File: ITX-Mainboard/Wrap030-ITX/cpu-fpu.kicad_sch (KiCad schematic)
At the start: 36 parts, among them J2 Conn_01x03, U1 MC68882, X2 16M, X2 50M

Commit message: Schematic substantial completion
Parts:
- C1, C10, C11, C12, C13, C14, C2, C3, C31, C4, C5, C6, C7, C8, C9: footprint Capacitor_SMD:C_0805_2012Metric -> Capacitor_SMD:C_0402_1005Metric_Pad0.74x0.62mm_HandSolder; JLC-Part (none) -> https://jlcpcb.com/partdetail/1877-CL05B104KO5NNNC/C1525
- C15, C16: footprint Capacitor_SMD:C_0805_2012Metric -> Capacitor_SMD:C_0402_1005Metric_Pad0.74x0.62mm_HandSolder; JLC-Part (none) -> https://jlcpcb.com/partdetail/53938-CL05A105KA5NQNC/C52923
- J2: footprint (none) -> Connector_PinHeader_2.54mm:PinHeader_1x03_P2.54mm_Vertical
- RN1: Mouser-Part (none) -> 603-YC164-FR-071KL; Notes (none) -> 1k x4

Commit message: PCB substantial completion
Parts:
- added R2: 10k, Resistor_SMD:R_0805_2012Metric, symbol Device:R_Small_US
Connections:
- net FPU-CLK: now also J2.2 (Pin_2), U1.C2 (CLK); no longer J2.3 (Pin_3), X2.5 (OUT)
- net VCC: now also R2.2
- net ~{AVEC}: now also RN1.3 (R3.1); no longer RN1.4 (R4.1)
- net ~{BERR}: now also RN1.3 (R3.1); no longer RN1.1 (R1.1)
- net ~{CBACK}: now also RN1.1 (R1.1); no longer RN1.2 (R2.1)
- net ~{CDIS}: now also RN1.1 (R1.1); no longer RN1.1 (R1.1)
- net ~{CIIN}: now also RN1.2 (R2.1); no longer RN1.1 (R1.1)
- net ~{DSACK0}: now also RN1.4 (R4.1); no longer RN1.3 (R3.1), U1.J4 (~{DSACK0})
- net ~{DSACK1}: now also RN1.1 (R1.1); no longer RN1.4 (R4.1), U1.K4 (~{DSACK1})
- net ~{FPU-SENSE}: now also R2.1; no longer RN1.4 (R4.1)
- net ~{HALT}: now also RN1.4 (R4.1); no longer RN1.3 (R3.1)
- net ~{IPL0}: now also RN1.2 (R2.1); no longer RN1.1 (R1.1)
- net ~{IPL1}: now also RN1.4 (R4.1); no longer RN1.2 (R2.1)
- net ~{RESET}: now also RN1.1 (R1.1); no longer RN1.2 (R2.1)
- net ~{STERM}: now also RN1.2 (R2.1); no longer RN1.3 (R3.1)
- new net FPU-OSC: J2.3 (Pin_3), X2.5 (OUT)
- new net ~{BUS-DSACK0}: U1.J4 (~{DSACK0})
- new net ~{BUS-DSACK1}: U1.K4 (~{DSACK1})

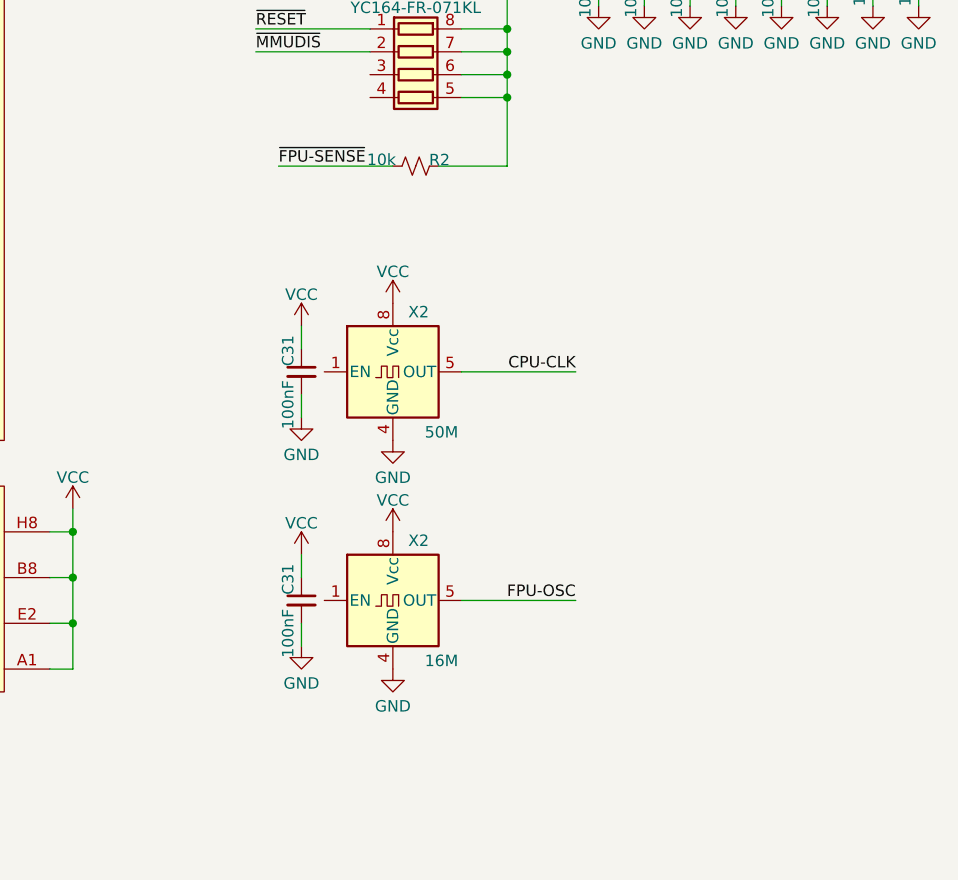
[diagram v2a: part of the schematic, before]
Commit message: Add interrupt controller to schematic
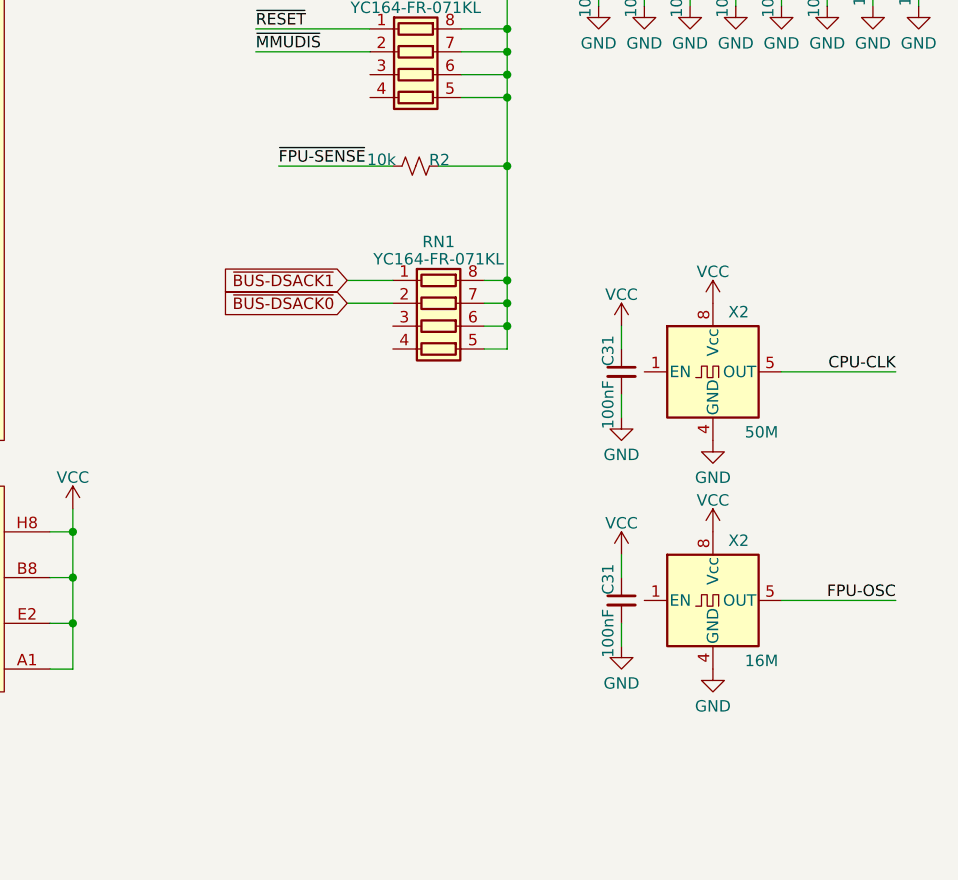
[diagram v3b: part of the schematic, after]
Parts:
- added RN1: YC164-FR-071KL, Resistor_SMD:R_Array_Convex_4x1206, symbol Device:R_Pack04
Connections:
- net VCC: now also RN1.5 (R4.2), RN1.6 (R3.2), RN1.7 (R2.2), RN1.8 (R1.2)
- net ~{BUS-DSACK0}: now also RN1.2 (R2.1)
- net ~{BUS-DSACK1}: now also RN1.1 (R1.1)
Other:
- moved on the sheet: C31, X2

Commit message: Completing PCB Routing
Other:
- title: Wrap030 ITX -> Wrap030-ATX Mainboard
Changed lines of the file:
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@@
   (paper "USLetter")
   (title_block
-    (title "Wrap030 ITX")
-    (date "2023-03-15")
-    (rev "0")
+    (title "Wrap030-ATX Mainboard")
+    (date "2023-03-26")
+    (rev "1")
     (company "techav")
   )

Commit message: initial production schematic
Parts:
- J2: value Conn_01x03 -> FPU CLK
- R2: JLC-Part (none) -> https://jlcpcb.com/partdetail/18102-0805W8F1002T5E/C17414
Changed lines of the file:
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@@
       (effects (font (size 1.27 1.27)))
     )
-    (property "Value" "Conn_01x03" (at 121.92 15.4211 0)
+    (property "Value" "FPU CLK" (at 121.92 15.4211 0)
       (effects (font (size 1.27 1.27)))
     )
@@
       (effects (font (size 1.27 1.27)) hide)
     )
-    (property "JLC-Part" "" (at 205.74 101.6 0)
-      (effects (font (size 1.27 1.27)) hide)
-    )
+    (property "JLC-Part" "https://jlcpcb.com/partdetail/18102-0805W8F1002T5E/C17414" (at 205.74 101.6 0)
+      (effects (font (size 1.27 1.27)) hide)
+    )

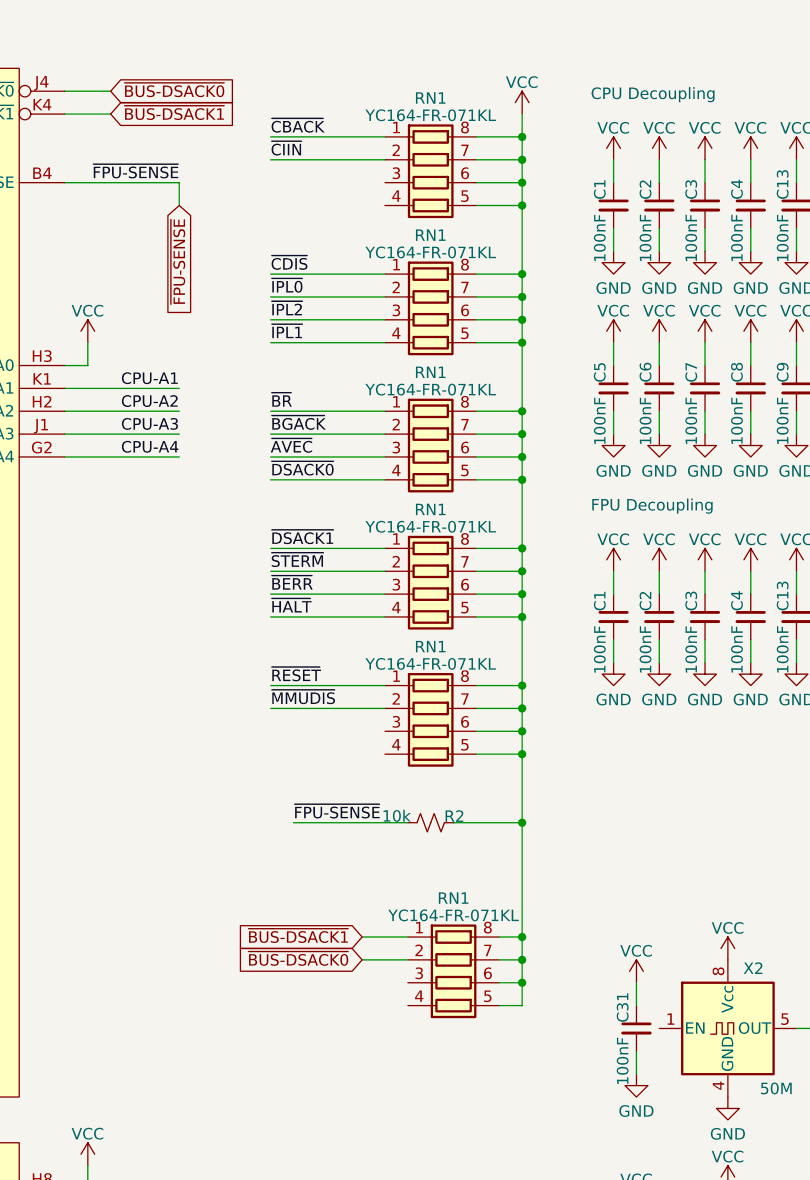
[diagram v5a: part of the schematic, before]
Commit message: Replace resistor nets with 0402 & update gerbers
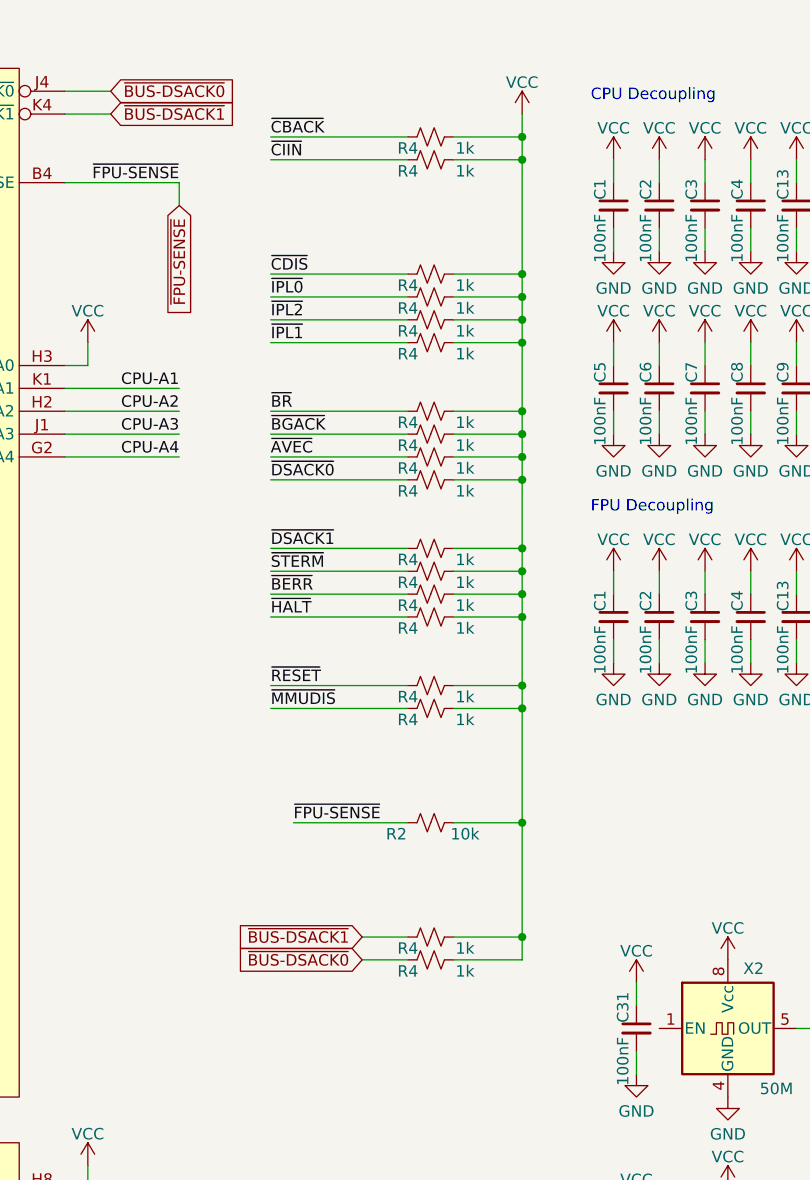
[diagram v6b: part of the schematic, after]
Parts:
- removed RN1 (x6): YC164-FR-071KL, Resistor_SMD:R_Array_Convex_4x1206, symbol Device:R_Pack04
- added R4 (x18): 1k, Resistor_SMD:R_0402_1005Metric_Pad0.72x0.64mm_HandSolder, symbol Device:R_Small_US
- C1, C10, C11, C12, C13, C14, C2, C3, C31, C4, C5, C6, C7, C8, C9: Mouser-Part (none) -> 187-CL05B104KO5NNNC; Notes (none) -> JLC
- C15, C16: Mouser-Part (none) -> 187-CL05A105KA5NQNC; Notes (none) -> JLC
- CPU1: Notes (none) -> OFE; Socket-Mouser (none) -> 437-5108712813041101
- J2: Mouser-Part (none) -> 523-G800W305018EU; Notes (none) -> OFE
- R2: footprint Resistor_SMD:R_0805_2012Metric -> Resistor_SMD:R_0402_1005Metric_Pad0.72x0.64mm_HandSolder; JLC-Part https://jlcpcb.com/partdetail/18102-0805W8F1002T5E/C17414 -> https://jlcpcb.com/partdetail/26487-0402WGF1002TCE/C25744; Mouser-Part (none) -> 303-0402WGF1002TCE; Notes (none) -> JLC
- U1: Notes (none) -> Mouser; Socket-Mouser (none) -> 437-5108306810061101
- X2: Mouser-Part (none) -> 815-ACH-50-EK; Notes (none) -> Mouser
- X2: Mouser-Part (none) -> 815-ACH-16-EK; Notes (none) -> Mouser
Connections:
- net VCC: now also R4.2, R4.2, R4.2, R4.2, R4.2, R4.2, R4.2, R4.2, R4.2, R4.2, R4.2, R4.2, R4.2, R4.2, R4.2, R4.2, R4.2, R4.2
- net ~{AVEC}: now also R4.1
- net ~{BERR}: now also R4.1
- net ~{BGACK}: now also R4.1
- net ~{BR}: now also R4.1
- net ~{BUS-DSACK0}: now also R4.1
- net ~{BUS-DSACK1}: now also R4.1
- net ~{CBACK}: now also R4.1
- net ~{CDIS}: now also R4.1
- net ~{CIIN}: now also R4.1
- net ~{DSACK0}: now also R4.1
- net ~{DSACK1}: now also R4.1
- net ~{HALT}: now also R4.1
- net ~{IPL0}: now also R4.1
- net ~{IPL1}: now also R4.1
- net ~{IPL2}: now also R4.1
- net ~{MMUDIS}: now also R4.1
- net ~{RESET}: now also R4.1
- net ~{STERM}: now also R4.1
